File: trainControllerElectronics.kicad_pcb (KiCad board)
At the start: 2 copper layers, 109.8 x 94.4 mm, 33 parts, among them IC1 IRF7606TRPBF, J1 ‎WM3436CT-ND‎, J2 USBC, J3 Battery, J4 Debug, J5 Serial, SW1 SW_MEC_5E, SW10 SW_MEC_5E, SW11 SW_MEC_5E, SW12 SW_MEC_5E, SW2 SW_MEC_5E, SW3 SW_MEC_5E, SW4 SW_MEC_5E, SW5 SW_MEC_5E, SW6 SW_MEC_5E, SW7 SW_MEC_5E, SW8 SW_MEC_5E, SW9 SW_MEC_5E, U1 CD74HC4067M96, U3 MCP73831-2-OT

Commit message: library cleaned
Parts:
- RV1, RV2, RV3, RV4: footprint Potentiometer_THT:Potentiometer_Bourns_PTV09A-1_Single_Vertical -> ptv09:Potentiometer_Bourns_PTV09A-1_Single_Vertical
- SW1, SW10, SW11, SW12, SW2, SW3, SW4, SW5, SW6, SW7, SW8, SW9: value SW_MEC_5E -> PTS647SM38SMTR2; footprint Button_Switch_SMD:SW_SPST_Omron_B3FS-101xP -> Button_Switch_SMD:SW_SPST_PTS647_Sx38
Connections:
- SW1 pad 1: unconnected-(SW1-Pad1) -> KEY_COL_1

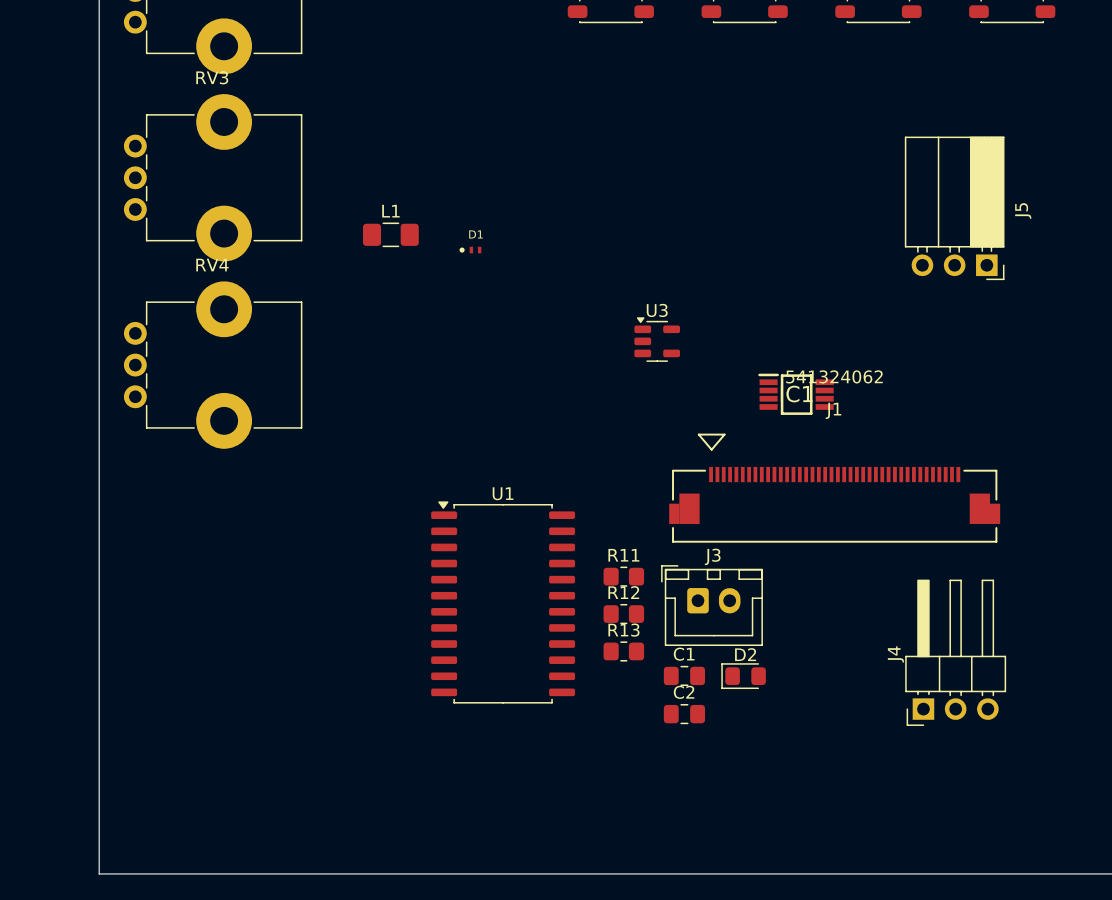
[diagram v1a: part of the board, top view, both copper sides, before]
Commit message: New mosfet
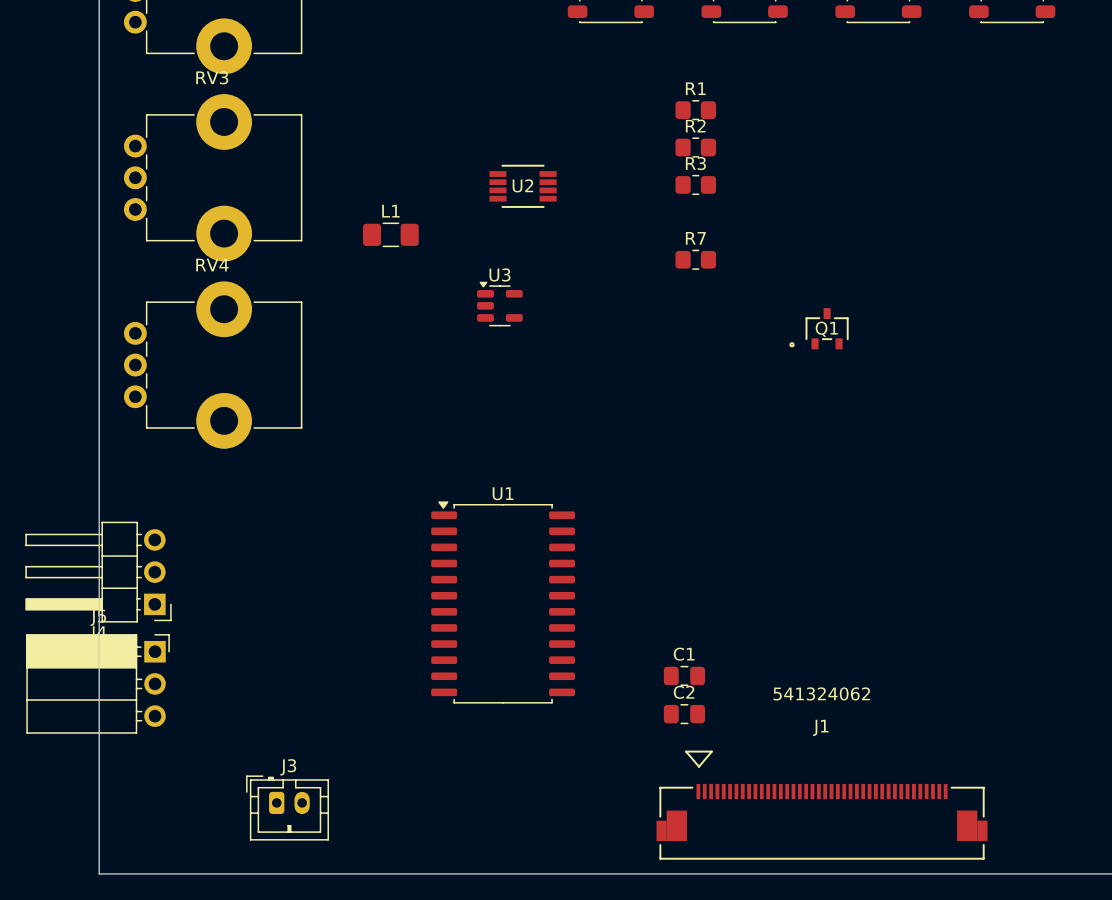
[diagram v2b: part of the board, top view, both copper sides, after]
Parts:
- removed D1: D_Schottky, PMEG4010AESBYL:DIODFN100X60X30-2N
- removed D2: RED, LED_SMD:LED_0805_2012Metric_Pad1.15x1.40mm_HandSolder
- removed IC1: IRF7606TRPBF, IRF7606TRPBF:SOP65P490X111-8N
- removed R11: 2K, Resistor_SMD:R_0805_2012Metric_Pad1.20x1.40mm_HandSolder
- removed R12: 330R, Resistor_SMD:R_0805_2012Metric_Pad1.20x1.40mm_HandSolder
- removed R13: 10K, Resistor_SMD:R_0805_2012Metric_Pad1.20x1.40mm_HandSolder
- added Q1: BSS670S2LH6327XTSA1, BSS670S2L:PG-SOT23-3-5_INF, F.Cu at (131.4, 94.0)
- added R1: 10K, Resistor_SMD:R_0805_2012Metric_Pad1.20x1.40mm_HandSolder, F.Cu at (121.0, 76.8)
- added R2: 2K, Resistor_SMD:R_0805_2012Metric_Pad1.20x1.40mm_HandSolder, F.Cu at (121.0, 79.7)
- added R3: 10K, Resistor_SMD:R_0805_2012Metric_Pad1.20x1.40mm_HandSolder, F.Cu at (121.0, 82.7)
- added R7: 0R, Resistor_SMD:R_0805_2012Metric_Pad1.20x1.40mm_HandSolder, F.Cu at (121.0, 88.6)
- added U2: ZXM64P03XTA, ZXM64P03XTA:SOIC8_ZXM64P03X_DIO, F.Cu at (107.4, 82.8)
- A1: value RaspberryPi_Pico_W -> SC0918 RaspberryPi Pico W
- J1: value ‎WM3436CT-ND‎ -> 0541324062
- J2: value USBC -> USB4135-GF-A
- J3: value Battery -> B2B-PH-K-S; footprint Connector_JST:JST_XH_B2B-XH-A_1x02_P2.50mm_Vertical -> Connector_JST:JST_PH_B2B-PH-K_1x02_P2.00mm_Vertical
- J4: value Debug -> Pin header 2.54 1x03
- J5: value Serial -> Pin socket 2.54 1x03
- RV1, RV2, RV3, RV4: value 20K -> PTV09A-4015F-B104‎
- SW1, SW10, SW11, SW12, SW2, SW3, SW4, SW5, SW6, SW7, SW8, SW9: value PTS647SM38SMTR2 -> PTS647SM38SMTR2 LFS
- U3: value MCP73831-2-OT -> MCP73831T-2ACI/OT
- moved J5 72.3 mm to (78.4, 119.5), turned to 0 degrees
- moved J4 61.2 mm to (78.4, 115.7), turned to 180 degrees
- moved J3 36.8 mm to (88.0, 131.4)
- moved J1 25.0 mm to (131.0, 133.0)
- moved U3 12.7 mm to (105.6, 92.2)
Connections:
- A1 pad 10: Display_D2 -> Display_D1
- A1 pad 11: Display_D3 -> Display_D2
- A1 pad 12: Display_D4 -> Display_D3
- A1 pad 14: Display_D5 -> Display_D4
- A1 pad 15: Display_D6 -> Display_D5
- A1 pad 16: Display_D7 -> Display_D6
- A1 pad 17: Analog_SW_D0 -> Display_D7
- A1 pad 19: Analog_SW_D1 -> Analog_SW_D0
- A1 pad 20: Analog_SW_D2 -> Analog_SW_D1
- A1 pad 34: unconnected-(A1-GPIO28_ADC2-Pad34) -> BATT_STAT
- A1 pad 39: +5v -> Vsys
- A1 pad 40: unconnected-(A1-VBUS-Pad40) -> Vbus
- A1 pad 7: Display_D0 -> Backlight_PWM
- A1 pad 9: Display_D1 -> Display_D0
- C1 pad 1: Net-(D1-A) -> Vbus
- C2 pad 1: Net-(IC1-S_1) -> Net-(J3-Pin_1)
- J1 pad 34: GND -> Net-(Q1-D)
- J1 pad 35: GND -> Net-(Q1-D)
- J1 pad 36: GND -> Net-(Q1-D)
- J1 pad 37: GND -> Net-(Q1-D)
- J3 pad 1: GND -> Net-(J3-Pin_1)
- J3 pad 2: Net-(IC1-S_1) -> GND
- L1 pad 2: Net-(D1-A) -> Vbus
- RV2 pad 2: Net-(U1-I2) -> Net-(U1-I1)
- RV3 pad 2: Net-(U1-I1) -> Net-(U1-I2)
- U1 pad 14: Analog_SW_D2 -> GND
- U3 pad 1: Net-(D2-A) -> BATT_STAT
- U3 pad 3: Net-(IC1-S_1) -> Net-(J3-Pin_1)
- U3 pad 4: Net-(D1-A) -> Vbus

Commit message: Added Battery meter
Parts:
- added R4: 10K, Resistor_SMD:R_0805_2012Metric_Pad1.20x1.40mm_HandSolder, F.Cu at (137.4, 81.7)
- added R5: 10K, Resistor_SMD:R_0805_2012Metric_Pad1.20x1.40mm_HandSolder, F.Cu at (137.4, 84.6)
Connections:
- net Net-(J3-Pin_1) renamed BATT
- A1 pad 32: unconnected-(A1-GPIO27_ADC1-Pad32) -> Net-(A1-GPIO27_ADC1)

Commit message: PCB ready
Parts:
- removed A1: SC0918 RaspberryPi Pico W, Module:RaspberryPi_Pico_W_SMD_HandSolder
- removed Q1: BSS670S2LH6327XTSA1, BSS670S2L:PG-SOT23-3-5_INF
- removed SW10, SW11, SW12, SW8, SW9: PTS647SM38SMTR2 LFS, Button_Switch_SMD:SW_SPST_PTS647_Sx38
- added C3: 10u, Capacitor_SMD:C_0805_2012Metric_Pad1.18x1.45mm_HandSolder, B.Cu at (115.6, 101.5)
- added C4: 0.1u, Capacitor_SMD:C_0805_2012Metric_Pad1.18x1.45mm_HandSolder, B.Cu at (115.6, 94.3)
- added C5: 1u, Capacitor_SMD:C_0805_2012Metric_Pad1.18x1.45mm_HandSolder, B.Cu at (71.5, 105.4)
- added D1: SS15, Diode_SMD:D_SMA, B.Cu at (226.8, 67.8)
- added D2: SS15, Diode_SMD:D_SMA, B.Cu at (56.7, 118.6)
- added H1: MountingHole, MountingHole:MountingHole_3.2mm_M3_Pad_Via, F.Cu at (43.9, 57.7)
- added H2: MountingHole, MountingHole:MountingHole_3.2mm_M3_Pad_Via, F.Cu at (200.3, 84.6)
- added H3: MountingHole, MountingHole:MountingHole_3.2mm_M3_Pad_Via, F.Cu at (43.9, 113.1)
- added R10: 1K, Resistor_SMD:R_0805_2012Metric_Pad1.20x1.40mm_HandSolder, B.Cu at (235.1, 61.6)
- added R11: 0R, Resistor_SMD:R_0805_2012Metric_Pad1.20x1.40mm_HandSolder, B.Cu at (115.6, 90.8)
- added R12: 100K, Resistor_SMD:R_0805_2012Metric_Pad1.20x1.40mm_HandSolder, B.Cu at (65.9, 109.1)
- added R13: 100K, Resistor_SMD:R_0805_2012Metric_Pad1.20x1.40mm_HandSolder, B.Cu at (115.6, 97.8)
- added R14: 10K, Resistor_SMD:R_0805_2012Metric_Pad1.20x1.40mm_HandSolder, B.Cu at (66.0, 98.2)
- added R15: 1K, Resistor_SMD:R_0805_2012Metric_Pad1.20x1.40mm_HandSolder, B.Cu at (66.0, 101.8)
- added R16: 100K, Resistor_SMD:R_0805_2012Metric_Pad1.20x1.40mm_HandSolder, B.Cu at (65.9, 112.8)
- added R17: 100K, Resistor_SMD:R_0805_2012Metric_Pad1.20x1.40mm_HandSolder, B.Cu at (112.3, 116.6)
- added R18: 100K, Resistor_SMD:R_0805_2012Metric_Pad1.20x1.40mm_HandSolder, B.Cu at (112.3, 113.2)
- added R19: 0R, Resistor_SMD:R_0805_2012Metric_Pad1.20x1.40mm_HandSolder, B.Cu at (65.9, 105.3)
- added R6: 0R, Resistor_SMD:R_0805_2012Metric_Pad1.20x1.40mm_HandSolder, B.Cu at (76.7, 108.8)
- added R8: 10K, Resistor_SMD:R_0805_2012Metric_Pad1.20x1.40mm_HandSolder, B.Cu at (240.6, 71.0)
- added R9: 10K, Resistor_SMD:R_0805_2012Metric_Pad1.20x1.40mm_HandSolder, B.Cu at (235.1, 58.2)
- added REF**: OSHW-Logo2_9.8x8mm_SilkScreen, Symbol:OSHW-Logo2_9.8x8mm_SilkScreen, B.Cu at (160.2, 83.2)
- added U4: IRF7319TRPBF, IRF7319:TRANS_IRF7103TRPBF_INF, B.Cu at (227.2, 61.7)
- added U5: IRF7319TRPBF, IRF7319:TRANS_IRF7103TRPBF_INF, B.Cu at (112.3, 107.9)
- C1, C2, L1, R1, R3, R4, U1, U3: moved to B.Cu
- J1: value 0541324062 -> Pin socket 2.54 1x03; footprint WM3436CT-ND‎:CON_541324062_MOL -> Connector_PinSocket_2.54mm:PinSocket_1x03_P2.54mm_Horizontal; moved to B.Cu
- J2: value USB4135-GF-A -> Pin header 2.54 1x03; footprint Connector_USB:USB_C_Receptacle_GCT_USB4135-GF-A_6P_TopMnt_Horizontal -> Connector_PinHeader_2.54mm:PinHeader_1x03_P2.54mm_Horizontal; moved to B.Cu
- J3: value B2B-PH-K-S -> 0541324062; footprint Connector_JST:JST_PH_B2B-PH-K_1x02_P2.00mm_Vertical -> WM3436CT-ND‎:CON_541324062_MOL; moved to B.Cu
- J4: value Pin header 2.54 1x03 -> USB4135-GF-A; footprint Connector_PinHeader_2.54mm:PinHeader_1x03_P2.54mm_Horizontal -> Connector_USB:USB_C_Receptacle_GCT_USB4135-GF-A_6P_TopMnt_Horizontal; moved to B.Cu
- J5: value Pin socket 2.54 1x03 -> B2B-PH-K-S; footprint Connector_PinSocket_2.54mm:PinSocket_1x03_P2.54mm_Horizontal -> Connector_JST:JST_PH_B2B-PH-K_1x02_P2.00mm_Vertical; moved to B.Cu
- R2: value 2K -> 10K; moved to B.Cu
- R5: value 10K -> 0R; moved to B.Cu
- R7: value 0R -> 1K; moved to B.Cu
- SW1, SW2, SW3, SW4, SW5, SW6, SW7: value PTS647SM38SMTR2 LFS -> 1825910-6; footprint Button_Switch_SMD:SW_SPST_PTS647_Sx38 -> Button_Switch_THT:SW_PUSH_6mm
- U2: value ZXM64P03XTA -> SC0918 RaspberryPi Pico W; footprint ZXM64P03XTA:SOIC8_ZXM64P03X_DIO -> Module:RaspberryPi_Pico_W_SMD_HandSolder; moved to B.Cu
- moved J4 184.2 mm to (253.0, 57.2), turned to -90 degrees
- moved J5 176.3 mm to (246.9, 67.5), turned to -90 degrees
- moved RV2 168.7 mm to (235.1, 128.1), turned to 90 degrees
- moved RV1 165.0 mm to (239.6, 82.1), turned to 180 degrees
- moved J2 164.8 mm to (252.3, 106.5), turned to 0 degrees
- moved L1 148.9 mm to (243.2, 58.3), turned to 180 degrees
- moved U3 138.5 mm to (240.9, 62.7), turned to 180 degrees
- moved C2 133.1 mm to (240.6, 67.6)
- moved C1 129.1 mm to (240.6, 74.9)
- moved J1 127.8 mm to (252.3, 92.6), turned to 180 degrees
- moved R7 116.5 mm to (235.1, 65.0)
- moved SW7 103.3 mm to (54.6, 114.6), turned to 90 degrees
- moved R2 97.4 mm to (217.4, 66.0)
- moved R3 96.7 mm to (217.4, 75.0), turned to 180 degrees
- moved R1 96.6 mm to (217.4, 70.5)
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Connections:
- C1 pad 1: Vbus -> Net-(D1-A)
- C2 pad 1: BATT -> Vbat
- J1 pad 1: GND -> UART0_TX
- J1 pad 2: unconnected-(J1-Pad2) -> GND
- J1 pad 3: unconnected-(J1-Pad3) -> UART0_RX
- J3 pad 1: BATT -> GND
- J3 pad 2: GND -> unconnected-(J3-Pad2)
- J5 pad 1: UART0_TX -> Vbat
- L1 pad 1: Net-(J2-VBUS-PadA9) -> Net-(J4-VBUS-PadA9)
- L1 pad 2: Vbus -> Net-(D1-A)
- R1 pad 1: GND -> Net-(U2-GPIO26_ADC0)
- R1 pad 2: Vbus -> Vbat
- R2 pad 1: GND -> Net-(U2-GPIO27_ADC1)
- R2 pad 2: Net-(U3-PROG) -> BATT_STAT
- R3 pad 1: Backlight_PWM -> GND
- R3 pad 2: GND -> Net-(U2-GPIO26_ADC0)
- R4 pad 1: Net-(A1-GPIO27_ADC1) -> GND
- R4 pad 2: BATT -> Net-(U2-GPIO27_ADC1)
- R5 pad 1: GND -> Net-(J3-Pad34)
- R5 pad 2: Net-(A1-GPIO27_ADC1) -> Backlight_Cathode
- R7 pad 1: Net-(Q1-D) -> Net-(R10-Pad2)
- R7 pad 2: GND -> Net-(U3-PROG)
- SW2 pad 1: KEY_COL_1 -> KEY_COL_2
- SW2 pad 2: KEY_ROW_2 -> KEY_ROW_1
- SW3 pad 1: KEY_COL_1 -> KEY_COL_3
- SW3 pad 2: KEY_ROW_3 -> KEY_ROW_1
- SW4 pad 2: KEY_ROW_4 -> KEY_ROW_2
- SW5 pad 2: KEY_ROW_1 -> KEY_ROW_2
- SW6 pad 1: KEY_COL_2 -> KEY_COL_3
- SW7 pad 1: KEY_COL_2 -> Net-(D2-K)
- SW7 pad 2: KEY_ROW_3 -> GND
- U1 pad 1: ADC0 -> ADC2
- U1 pad 16: GND -> AGND
- U1 pad 17: GND -> AGND
- U1 pad 18: GND -> AGND
- U1 pad 19: GND -> AGND
- U1 pad 2: GND -> AGND
- U1 pad 20: GND -> AGND
- U1 pad 21: GND -> AGND
- U1 pad 22: GND -> AGND
- U1 pad 23: GND -> AGND
- U1 pad 3: GND -> AGND
- U1 pad 4: GND -> AGND
- U1 pad 5: GND -> AGND
- U2 pad 1: BATT -> UART0_TX
- U2 pad 2: BATT -> UART0_RX
- U2 pad 3: BATT -> GND
- U2 pad 4: Vbus -> Display_WR
- U2 pad 5: Vsys -> Display_DC
- U2 pad 6: Vsys -> Display_RST
- U2 pad 7: Vsys -> Backlight_PWM
- U2 pad 8: Vsys -> GND
- U3 pad 3: BATT -> Vbat
- U3 pad 4: Vbus -> Net-(D1-A)
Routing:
- net UART0_RX: track 0.00 -> 249.2 mm, vias 0 -> 1
- net UART0_TX: track 0.00 -> 236.3 mm, vias 0 -> 1
- net SWCK: track 0.00 -> 209.5 mm
- net Net-(D1-K): track 0.00 -> 207.4 mm, vias 0 -> 4
- net SWIO: track 0.00 -> 200.4 mm
- net ADC_VREF: track 0.00 -> 195.5 mm
- net Backlight_Cathode: track 0.00 -> 172.4 mm, vias 0 -> 2
- net Backlight_PWM: track 0.00 -> 160.7 mm, vias 0 -> 2
- net +3.3V: track 0.00 -> 142.2 mm, vias 0 -> 2
- net KEY_COL_3: track 0.00 -> 133.5 mm, vias 0 -> 1
- net Net-(U2-GPIO26_ADC0): track 0.00 -> 132.9 mm, vias 0 -> 2
- net KEY_COL_2: track 0.00 -> 131.7 mm, vias 0 -> 2
- net Net-(U2-GPIO27_ADC1): track 0.00 -> 129.7 mm, vias 0 -> 2
- net KEY_ROW_2: track 0.00 -> 121.6 mm, vias 0 -> 1
- net KEY_ROW_1: track 0.00 -> 100.6 mm, vias 0 -> 1
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- added copper zone on B.Cu, net AGND
- added copper zone on F.Cu, net AGND
- added copper zone on B.Cu, net GND
- added copper zone on F.Cu, net GND
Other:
- board size 109.8 x 94.4 mm -> 218 x 92.9 mm
- board text added: "Black -"
- board text added: "CAUTION Inverting battery polarity may cause fire or explossion"
- board text added: "RED +"
- board text added: "Rick's Train controller Version 1.0"
